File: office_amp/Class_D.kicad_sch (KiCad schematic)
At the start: 52 parts, among them J7 Screw_Terminal_01x04, Q6 BC856, Q7 BC850, Q8 BC856, Q9 BC856, U10 DS1882E, U12 TL082, U6 TPA3123D2

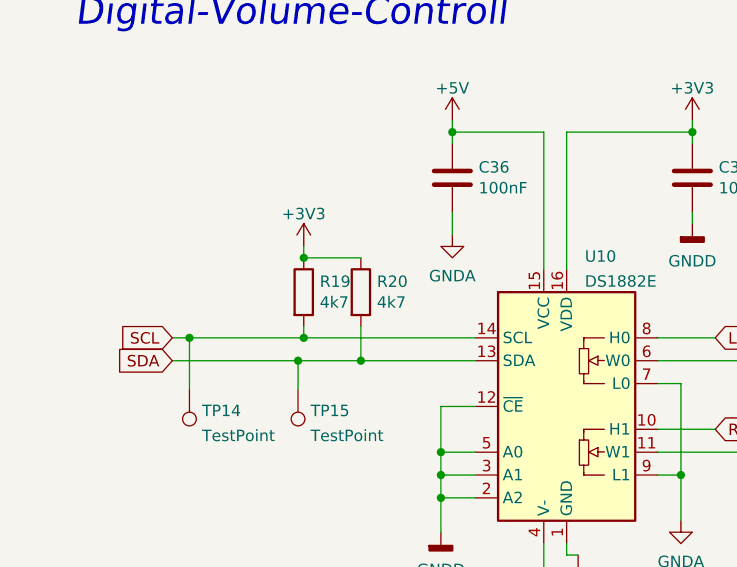
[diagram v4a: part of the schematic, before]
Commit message: Added bluetooth vcc filter, moved i2c pullups to controll board, added touch controller
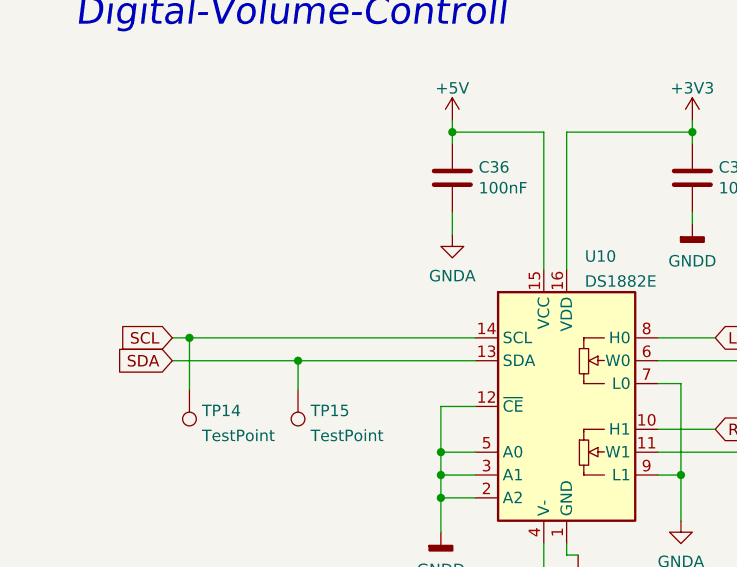
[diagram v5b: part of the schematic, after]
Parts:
- removed R19, R20: 4k7, Resistor_SMD:R_0805_2012Metric_Pad1.20x1.40mm_HandSolder, symbol Device:R
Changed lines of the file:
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@@
   (junction (at 218.44 110.49) (diameter 0) (color 0 0 0 0)
   )
-  (junction (at 44.45 186.69) (diameter 0) (color 0 0 0 0)
-  )
   (junction (at 86.36 201.93) (diameter 0) (color 0 0 0 0)
   )
-  (junction (at 50.8 189.23) (diameter 0) (color 0 0 0 0)
-  )
   (junction (at 196.85 29.21) (diameter 0) (color 0 0 0 0)
   )
@@
   (junction (at 166.37 40.64) (diameter 0) (color 0 0 0 0)
   )
-  (junction (at 44.45 177.8) (diameter 0) (color 0 0 0 0)
-  )
   (junction (at 248.92 105.41) (diameter 0) (color 0 0 0 0)
   )
@@
     (stroke (width 0) (type default) (color 0 0 0 0))
   )
-  (wire (pts (xy 50.8 185.42) (xy 50.8 189.23))
-    (stroke (width 0) (type default) (color 0 0 0 0))
-  )
   (wire (pts (xy 31.75 192.405) (xy 31.75 186.69))
     (stroke (width 0) (type default) (color 0 0 0 0))
@@
     (stroke (width 0) (type default) (color 0 0 0 0))
   )
-  (wire (pts (xy 44.45 176.53) (xy 44.45 177.8))
-    (stroke (width 0) (type default) (color 0 0 0 0))
-  )
   (wire (pts (xy 66.04 41.91) (xy 67.31 41.91))
     (stroke (width 0) (type default) (color 0 0 0 0))
@@
     (stroke (width 0) (type default) (color 0 0 0 0))
   )
-  (wire (pts (xy 44.45 185.42) (xy 44.45 186.69))
-    (stroke (width 0) (type default) (color 0 0 0 0))
-  )
   (wire (pts (xy 97.79 189.23) (xy 97.79 177.8))
     (stroke (width 0) (type default) (color 0 0 0 0))
@@
     (stroke (width 0) (type default) (color 0 0 0 0))
   )
-  (wire (pts (xy 50.8 189.23) (xy 63.5 189.23))
-    (stroke (width 0) (type default) (color 0 0 0 0))
-  )
   (wire (pts (xy 54.61 217.17) (xy 54.61 214.63))
     (stroke (width 0) (type default) (color 0 0 0 0))
@@
     (stroke (width 0) (type default) (color 0 0 0 0))
   )
-  (wire (pts (xy 31.75 186.69) (xy 44.45 186.69))
+  (wire (pts (xy 31.75 186.69) (xy 63.5 186.69))
     (stroke (width 0) (type default) (color 0 0 0 0))
   )
@@
     (stroke (width 0) (type default) (color 0 0 0 0))
   )
-  (wire (pts (xy 44.45 186.69) (xy 63.5 186.69))
-    (stroke (width 0) (type default) (color 0 0 0 0))
-  )
   (wire (pts (xy 73.66 209.55) (xy 73.66 210.82))
     (stroke (width 0) (type default) (color 0 0 0 0))
@@
     (stroke (width 0) (type default) (color 0 0 0 0))
   )
-  (wire (pts (xy 43.815 189.23) (xy 50.8 189.23))
+  (wire (pts (xy 43.815 189.23) (xy 63.5 189.23))
     (stroke (width 0) (type default) (color 0 0 0 0))
   )
@@
   )
   (wire (pts (xy 124.46 104.14) (xy 124.46 106.68))
-    (stroke (width 0) (type default) (color 0 0 0 0))
-  )
-  (wire (pts (xy 50.8 177.8) (xy 44.45 177.8))
     (stroke (width 0) (type default) (color 0 0 0 0))
   )
@@
     (pin "1")
   )
-  (symbol (lib_id "power:+3V3") (at 44.45 176.53 0) (unit 1)
-    (in_bom yes) (on_board yes) (fields_autoplaced)
-    (property "Reference" "#PWR055" (id 0) (at 44.45 180.34 0)
-      (effects (font (size 1.27 1.27)) hide)
-    )
-    (property "Value" "+3V3" (id 1) (at 44.45 172.9255 0))
-    (property "Footprint" "" (id 2) (at 44.45 176.53 0)
-      (effects (font (size 1.27 1.27)) hide)
-    )
-    (property "Datasheet" "" (id 3) (at 44.45 176.53 0)
-      (effects (font (size 1.27 1.27)) hide)
-    )
-    (pin "1")
-  )
   (symbol (lib_id "power:-5V") (at 60.96 229.87 180) (unit 1)
     (in_bom yes) (on_board yes)
@@
     )
     (property "Datasheet" "~" (id 3) (at 66.04 36.83 0)
-      (effects (font (size 1.27 1.27)) hide)
-    )
-    (pin "1")
-    (pin "2")
-  )
-  (symbol (lib_id "Device:R") (at 44.45 181.61 0) (unit 1)
-    (in_bom yes) (on_board yes)
-    (property "Reference" "R19" (id 0) (at 46.228 180.4416 0)
-      (effects (font (size 1.27 1.27)) (justify left))
-    )
-    (property "Value" "4k7" (id 1) (at 46.228 182.753 0)
-      (effects (font (size 1.27 1.27)) (justify left))
-    )
-    (property "Footprint" "Resistor_SMD:R_0805_2012Metric_Pad1.20x1.40mm_HandSolder" (id 2) (at 42.672 181.61 90)
-      (effects (font (size 1.27 1.27)) hide)
-    )
-    (property "Datasheet" "~" (id 3) (at 44.45 181.61 0)
       (effects (font (size 1.27 1.27)) hide)
     )
@@
     (pin "3")
   )
-  (symbol (lib_id "Device:R") (at 50.8 181.61 0) (unit 1)
-    (in_bom yes) (on_board yes)
-    (property "Reference" "R20" (id 0) (at 52.578 180.4416 0)
-      (effects (font (size 1.27 1.27)) (justify left))
-    )
-    (property "Value" "4k7" (id 1) (at 52.578 182.753 0)
-      (effects (font (size 1.27 1.27)) (justify left))
-    )
-    (property "Footprint" "Resistor_SMD:R_0805_2012Metric_Pad1.20x1.40mm_HandSolder" (id 2) (at 49.022 181.61 90)
-      (effects (font (size 1.27 1.27)) hide)
-    )
-    (property "Datasheet" "~" (id 3) (at 50.8 181.61 0)
-      (effects (font (size 1.27 1.27)) hide)
-    )
-    (pin "1")
-    (pin "2")
-  )
   (symbol (lib_id "Device:R") (at 115.57 90.17 180) (unit 1)

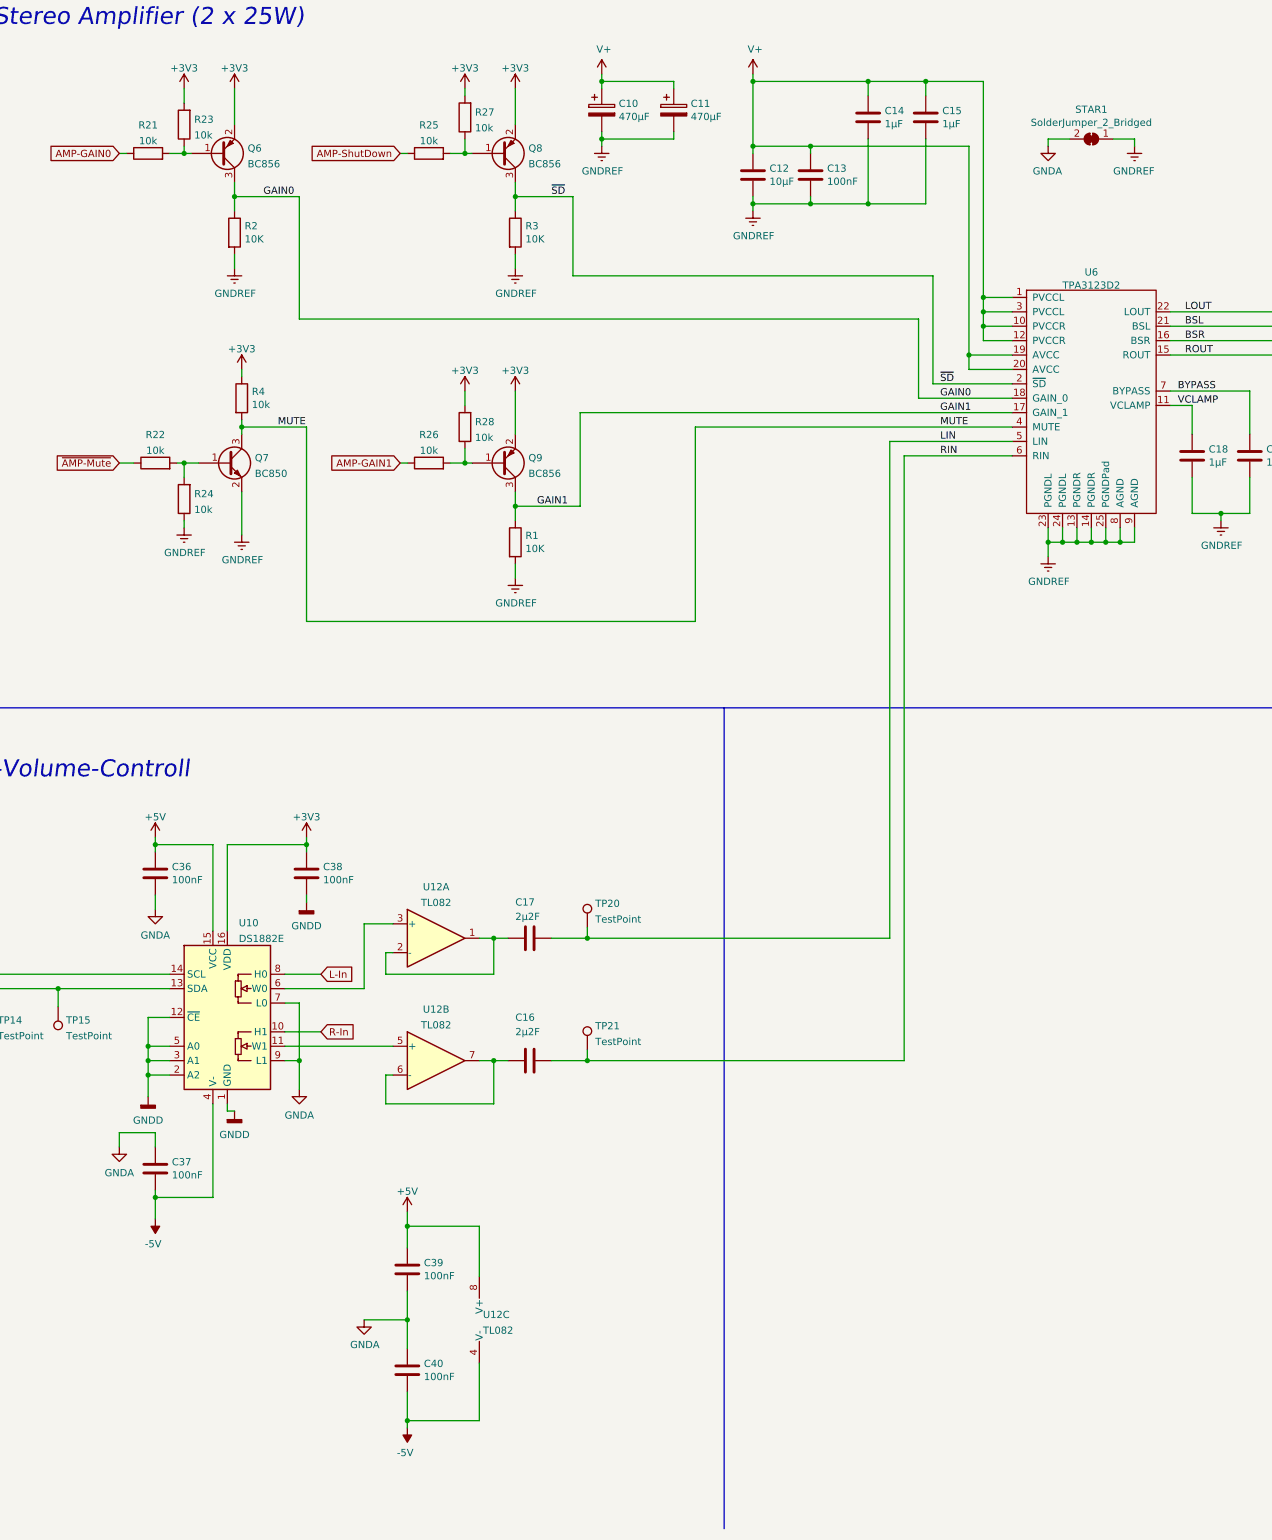
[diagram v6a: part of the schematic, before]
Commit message: Added CHanges from Testing, first layout V1.5
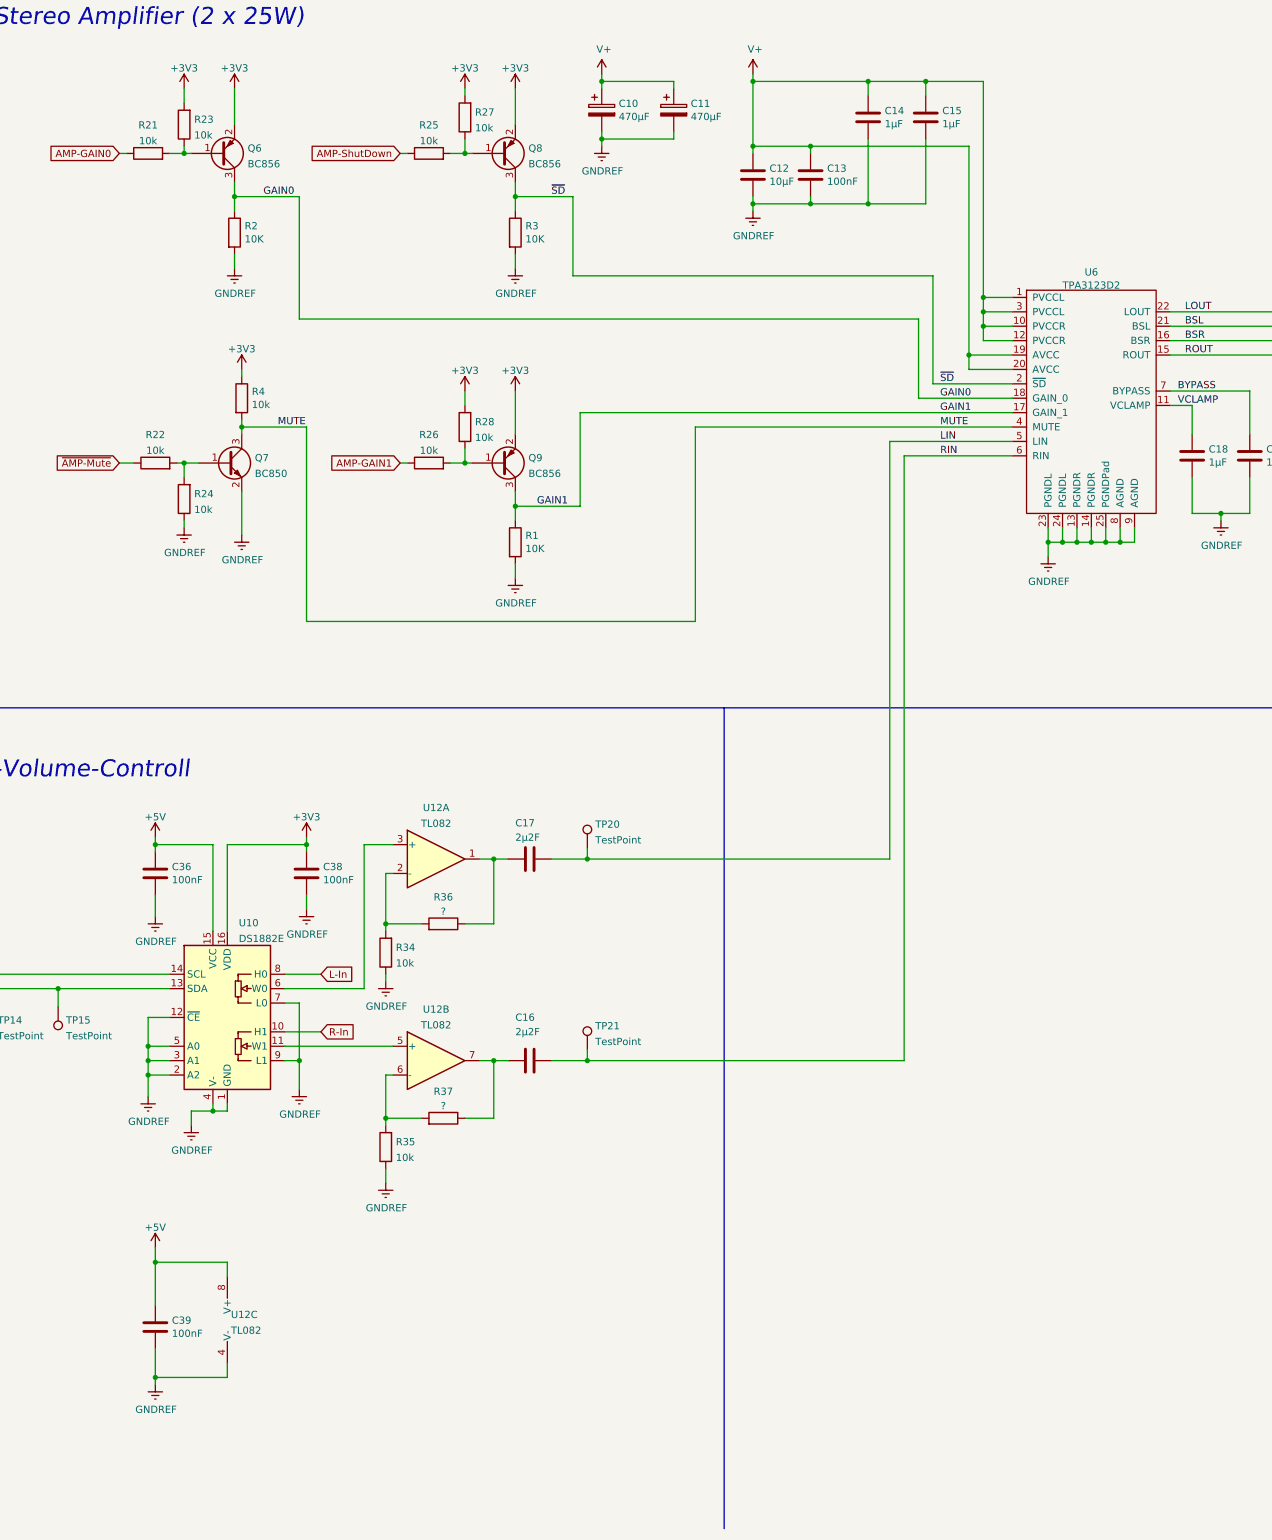
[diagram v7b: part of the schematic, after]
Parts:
- removed C37, C40: 100nF, Capacitor_SMD:C_0805_2012Metric_Pad1.18x1.45mm_HandSolder, symbol Device:C
- removed STAR1: SolderJumper_2_Bridged, Jumper:SolderJumper-2_P1.3mm_Bridged_RoundedPad1.0x1.5mm, symbol Jumper:SolderJumper_2_Bridged
- added R34, R35: 10k, Resistor_SMD:R_0805_2012Metric_Pad1.20x1.40mm_HandSolder, symbol Device:R
- added R36, R37: ?, Resistor_SMD:R_0805_2012Metric_Pad1.20x1.40mm_HandSolder, symbol Device:R
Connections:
- net -5V is gone; now on net GNDREF: U10.4 (V-), U12.4 (V-)
- net GNDA is gone; now on net GNDREF: C36.2, C39.2, U10.7 (L0), U10.9 (L1)
- net GNDD is gone; now on net GNDREF: C38.2, U10.1 (GND), U10.12 (~{CE}), U10.2 (A2), U10.3 (A1), U10.5 (A0)
- net GNDREF: now also R34.1, R35.1
- net at C16.2, U12.7: now also R37.1; no longer U12.6 (-)
- net at C17.2, U12.1: now also R36.1; no longer U12.2 (-)
- new net: R35.2, R37.2, U12.6 (-)
- new net: R34.2, R36.2, U12.2 (-)
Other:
- moved on the sheet: C17, C39, TP20, U12A, U12C
